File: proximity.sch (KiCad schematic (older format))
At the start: 5 parts, among them U1 TCRT1000

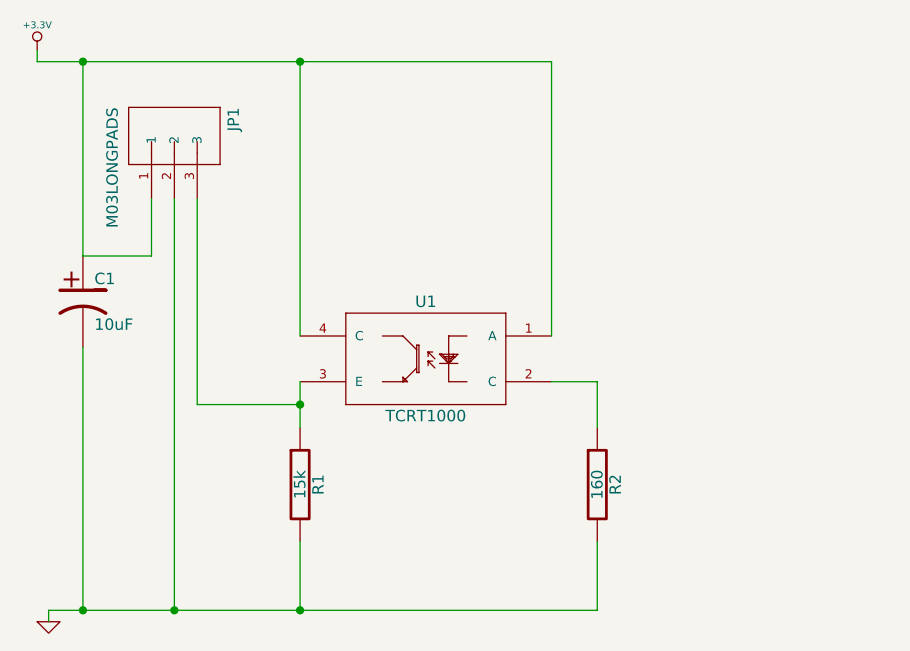
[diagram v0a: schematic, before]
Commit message: Changes made to allow firmware control of the emitter.
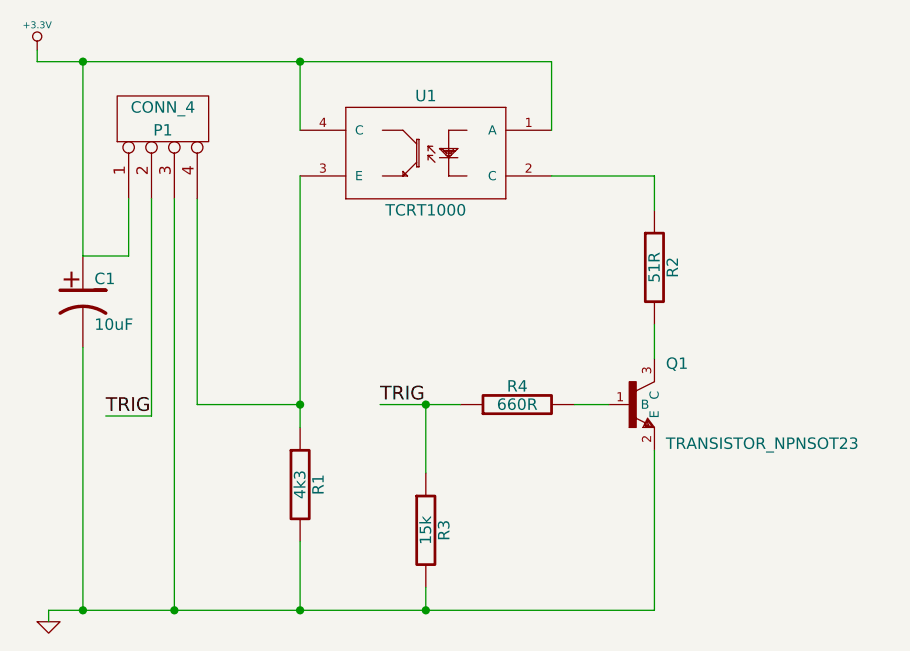
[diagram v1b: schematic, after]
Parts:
- removed JP1: M03LONGPADS, SparkFun-1X03_LONGPADS, symbol M03LONGPADS
- added P1: CONN_4, symbol CONN_4
- added Q1: TRANSISTOR_NPNSOT23, SparkFun-SOT23, symbol TRANSISTOR_NPNSOT23
- added R3: 15k, symbol R
- added R4: 660R, symbol R
- R1: value 15k -> 4k3
- R2: value 160 -> 51R
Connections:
- net +3.3V: now also P1.1 (P1)
- net GND: now also P1.3 (P3), Q1.2 (E), R3.2; no longer R2.2
- net at R1.1, U1.3 (E): now also P1.4 (P4)
- new net: Q1.3 (C), R2.2
- new net: Q1.1 (B), R4.2
- new net TRIG: P1.2 (P2), R3.1, R4.1
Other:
- moved on the sheet: R2, U1
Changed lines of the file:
@@
-EESchema Schematic File Version 2  date Wed 30 Oct 2013 20:10:22 GMT
+EESchema Schematic File Version 2  date Fri 10 Jan 2014 11:55:38 GMT
 LIBS:power
 LIBS:device
@@
 Sheet 1 1
 Title ""
-Date "22 oct 2013"
+Date "10 jan 2014"
 Rev ""
 Comp ""
@@
 Comment4 ""
 $EndDescr
+Wire Wire Line
+	2500 2800 2500 3900
+Wire Wire Line
+	3700 3800 3850 3800
+Wire Wire Line
+	3050 3800 3050 4100
+Wire Wire Line
+	4050 2950 4050 2800
+Wire Wire Line
+	4050 2800 3600 2800
+Wire Wire Line
+	2500 2600 2500 2300
+Wire Wire Line
+	1650 3850 1850 3850
+Wire Wire Line
+	1850 3850 1850 2900
+Wire Wire Line
+	1750 2900 1750 3150
+Wire Wire Line
+	1350 2300 3600 2300
+Wire Wire Line
+	1350 2300 1350 2250
+Wire Wire Line
+	1950 2900 1950 4700
+Connection ~ 1550 2300
+Wire Wire Line
+	1550 2300 1550 3150
+Connection ~ 2500 2300
+Wire Wire Line
+	1400 4750 1400 4700
+Wire Wire Line
+	2500 4700 2500 4400
+Wire Wire Line
+	2500 3800 2050 3800
+Connection ~ 2500 3800
+Connection ~ 1950 4700
+Connection ~ 2500 4700
+Wire Wire Line
+	2050 3800 2050 2900
+Wire Wire Line
+	1550 3550 1550 4700
 Connection ~ 1550 4700
 Wire Wire Line
-	1550 3550 1550 4700
-Wire Wire Line
-	1400 4700 3800 4700
-Wire Wire Line
-	2050 2900 2050 3800
-Wire Wire Line
-	1850 2900 1850 3150
-Connection ~ 2500 4700
-Connection ~ 1950 4700
-Connection ~ 2500 3800
-Wire Wire Line
-	2050 3800 2500 3800
-Wire Wire Line
-	2500 4700 2500 4400
-Wire Wire Line
-	1400 4700 1400 4750
-Wire Wire Line
-	2500 3700 2500 3900
-Wire Wire Line
-	3800 4700 3800 4400
-Connection ~ 2500 2300
-Wire Wire Line
-	3600 3700 3800 3700
-Wire Wire Line
-	3800 3700 3800 3900
-Wire Wire Line
-	2500 3500 2500 2300
-Wire Wire Line
-	3600 3500 3600 2300
-Wire Wire Line
-	1550 2300 1550 3150
-Wire Wire Line
-	1550 3150 1850 3150
-Connection ~ 1550 2300
-Wire Wire Line
-	1950 2900 1950 4700
-Wire Wire Line
-	1350 2250 1350 2300
-Wire Wire Line
-	1350 2300 3600 2300
+	1550 3150 1750 3150
+Wire Wire Line
+	3050 4600 3050 4700
+Connection ~ 3050 4700
+Wire Wire Line
+	3600 2300 3600 2600
+Wire Wire Line
+	4050 3450 4050 3600
+Wire Wire Line
+	2850 3800 3200 3800
+Connection ~ 3050 3800
+Wire Wire Line
+	1400 4700 4050 4700
+Wire Wire Line
+	4050 4700 4050 4000
+$Comp
+L R R3
+U 1 1 52CC6FDD
+P 3050 4350
+F 0 "R3" V 3130 4350 50  0000 C CNN
+F 1 "15k" V 3050 4350 50  0000 C CNN
+	1    3050 4350
+	1    0    0    -1
+$EndComp
+$Comp
+L R R4
+U 1 1 52CC6FC3
+P 3450 3800
+F 0 "R4" V 3530 3800 50  0000 C CNN
+F 1 "660R" V 3450 3800 50  0000 C CNN
+	1    3450 3800
+	0    -1   -1   0
+$EndComp
+Text Label 1650 3850 0    60   ~ 0
+TRIG
+Text Label 2850 3800 0    60   ~ 0
+TRIG
+$Comp
+L CONN_4 P1
+U 1 1 52CC6F03
+P 1900 2550
+F 0 "P1" V 1850 2550 50  0000 C CNN
+F 1 "CONN_4" V 1950 2550 50  0000 C CNN
+	1    1900 2550
+	0    -1   -1   0
+$EndComp
+$Comp
+L TRANSISTOR_NPNSOT23 Q1
+U 1 1 52CC6E8B
+P 3950 3800
+F 0 "Q1" H 4100 3950 50  0000 L BNN
+F 1 "TRANSISTOR_NPNSOT23" H 4100 3600 50  0000 L BNN
+F 2 "SparkFun-SOT23" H 4450 3800 50  0001 C CNN
+	1    3950 3800
+	1    0    0    -1
+$EndComp
 $Comp
 L CP1 C1
@@
 L TCRT1000 U1
 U 1 1 520A9E11
-P 3000 3600
-F 0 "U1" H 3050 3850 50  0000 C CNN
-F 1 "TCRT1000" H 3050 3350 50  0000 C CNN
-	1    3000 3600
-	1    0    0    -1
-$EndComp
-$Comp
-L M03LONGPADS JP1
-U 1 1 520A9AE3
-P 1950 2600
-F 0 "JP1" H 1850 2830 50  0000 L BNN
-F 1 "M03LONGPADS" H 1850 2300 50  0000 L BNN
-F 2 "SparkFun-1X03_LONGPADS" H 1950 2750 50  0001 C CNN
-	1    1950 2600
-	0    1    1    0
+P 3000 2700
+F 0 "U1" H 3050 2950 50  0000 C CNN
+F 1 "TCRT1000" H 3050 2450 50  0000 C CNN
+	1    3000 2700
+	1    0    0    -1
 $EndComp
 $Comp
@@
 L R R2
 U 1 1 50F70715
-P 3800 4150
-F 0 "R2" V 3880 4150 50  0000 C CNN
-F 1 "160" V 3800 4150 50  0000 C CNN
-	1    3800 4150
+P 4050 3200
+F 0 "R2" V 4130 3200 50  0000 C CNN
+F 1 "51R" V 4050 3200 50  0000 C CNN
+	1    4050 3200
 	1    0    0    -1
 $EndComp
@@
 P 2500 4150
 F 0 "R1" V 2580 4150 50  0000 C CNN
-F 1 "15k" V 2500 4150 50  0000 C CNN
+F 1 "4k3" V 2500 4150 50  0000 C CNN
 	1    2500 4150
 	1    0    0    -1

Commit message: edits to board layout.
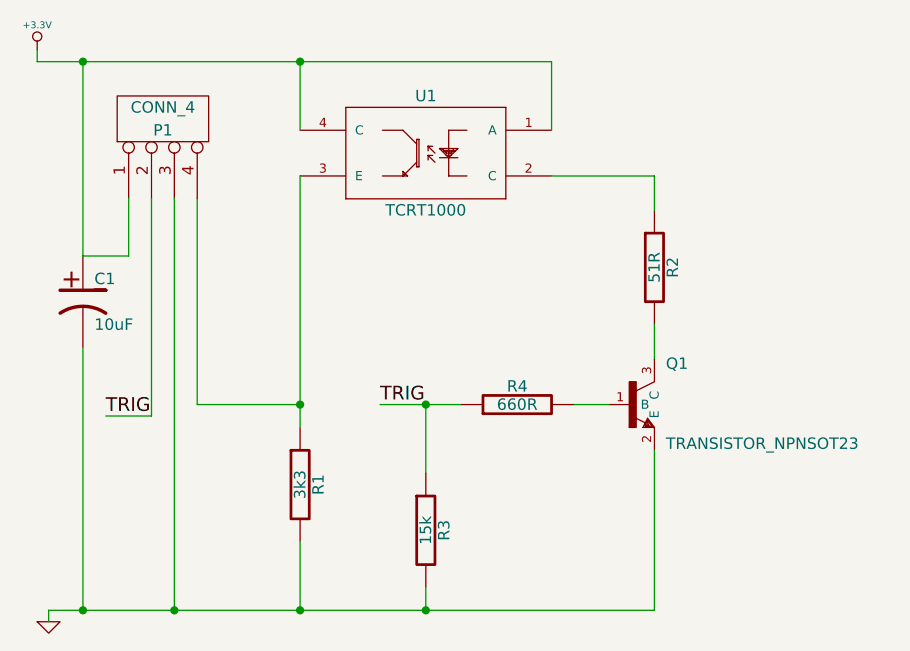
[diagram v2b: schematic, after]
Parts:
- R1: value 4k3 -> 3k3
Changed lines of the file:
@@
-EESchema Schematic File Version 2  date Fri 10 Jan 2014 11:55:38 GMT
+EESchema Schematic File Version 2  date Thu 23 Jan 2014 16:57:06 GMT
 LIBS:power
 LIBS:device
@@
 Sheet 1 1
 Title ""
-Date "10 jan 2014"
+Date "23 jan 2014"
 Rev ""
 Comp ""
@@
 P 2500 4150
 F 0 "R1" V 2580 4150 50  0000 C CNN
-F 1 "4k3" V 2500 4150 50  0000 C CNN
+F 1 "3k3" V 2500 4150 50  0000 C CNN
 	1    2500 4150
 	1    0    0    -1

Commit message: Emitter controlled by firmware. Files ready for manufacture, including GCode for PCB milling.
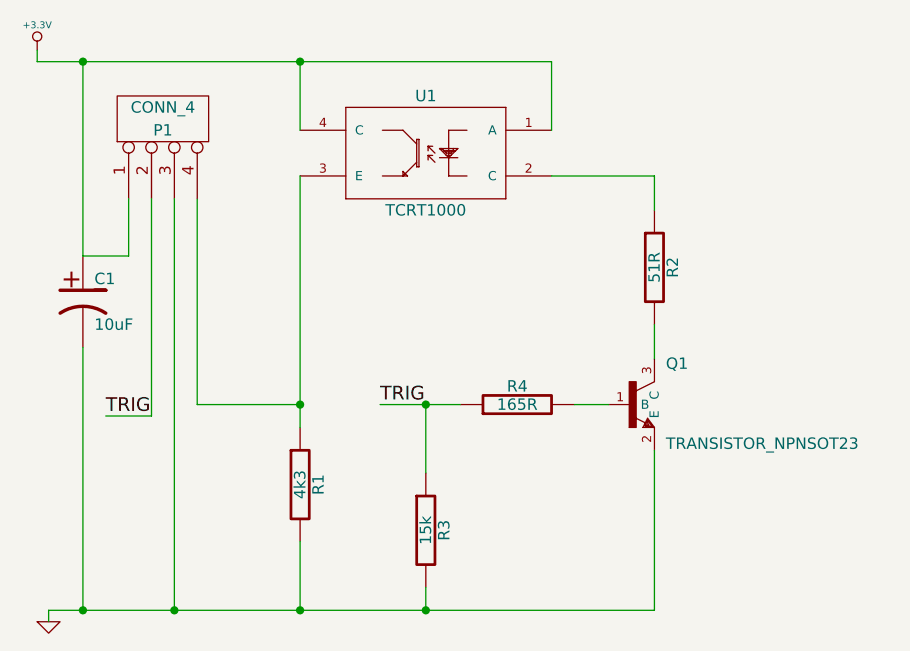
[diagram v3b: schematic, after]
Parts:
- R1: value 3k3 -> 4k3
- R4: value 660R -> 165R
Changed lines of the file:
@@
-EESchema Schematic File Version 2  date Thu 23 Jan 2014 16:57:06 GMT
+EESchema Schematic File Version 2  date Thu 17 Apr 2014 14:06:43 BST
 LIBS:power
 LIBS:device
@@
 Sheet 1 1
 Title ""
-Date "23 jan 2014"
+Date "17 apr 2014"
 Rev ""
 Comp ""
@@
 P 3450 3800
 F 0 "R4" V 3530 3800 50  0000 C CNN
-F 1 "660R" V 3450 3800 50  0000 C CNN
+F 1 "165R" V 3450 3800 50  0000 C CNN
 	1    3450 3800
 	0    -1   -1   0
@@
 P 2500 4150
 F 0 "R1" V 2580 4150 50  0000 C CNN
-F 1 "3k3" V 2500 4150 50  0000 C CNN
+F 1 "4k3" V 2500 4150 50  0000 C CNN
 	1    2500 4150
 	1    0    0    -1
